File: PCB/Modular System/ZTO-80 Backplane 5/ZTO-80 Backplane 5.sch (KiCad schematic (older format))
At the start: 25 parts, among them J1 ZTO-80 Bus, J10 Conn_01x02, J11 PJ-102A, J12 Conn_01x02, J13 Conn_01x02, J2 Conn_01x02, J3 ZTO-80 Bus, J4 Conn_01x02, J5 ZTO-80 Bus, J6 Conn_01x02, J7 ZTO-80 Bus, J8 Conn_01x02, J9 ZTO-80 Bus, SW1 Reset

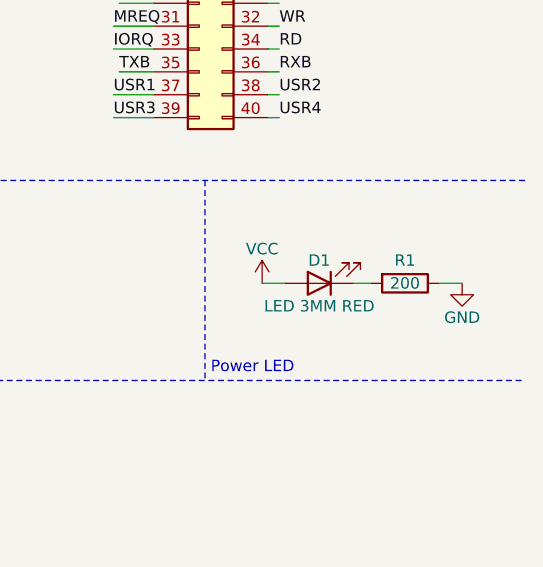
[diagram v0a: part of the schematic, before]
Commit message: Edited power LED resistor value
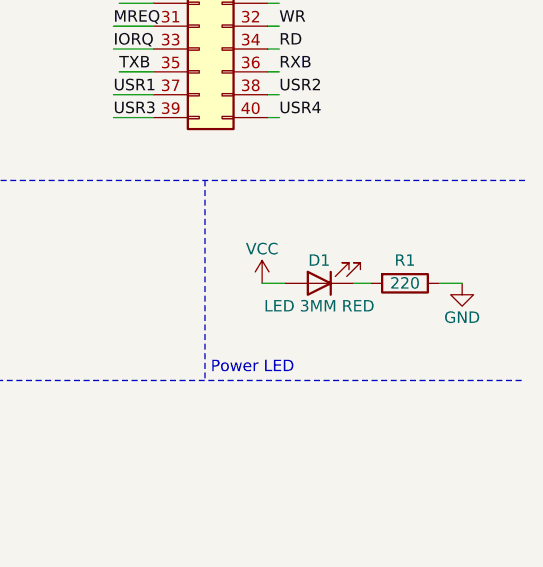
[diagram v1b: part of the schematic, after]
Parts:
- R1: value 200 -> 220
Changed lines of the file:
@@
 P 10700 3450
 F 0 "R1" V 10600 3450 50  0000 C CNN
-F 1 "200" V 10700 3450 50  0000 C CNN
+F 1 "220" V 10700 3450 50  0000 C CNN
 F 2 "Resistor_SMD:R_0805_2012Metric_Pad1.15x1.40mm_HandSolder" V 10630 3450 50  0001 C CNN
 F 3 "~" H 10700 3450 50  0001 C CNN

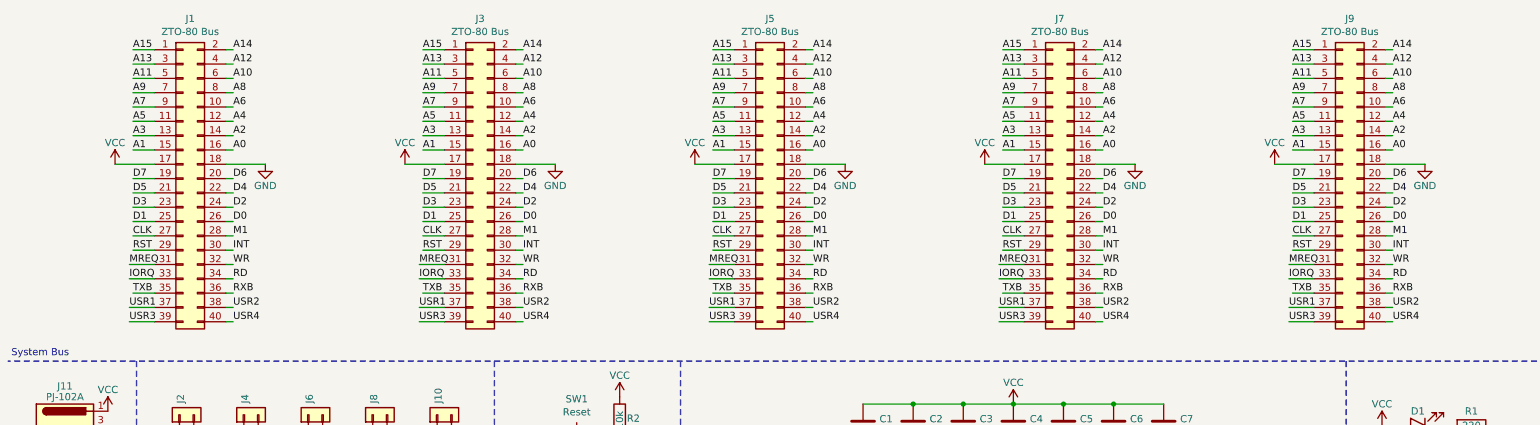
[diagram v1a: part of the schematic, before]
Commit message: Changed bus orientation
This change is backwards-compatible with all previous ZTO-80 modules
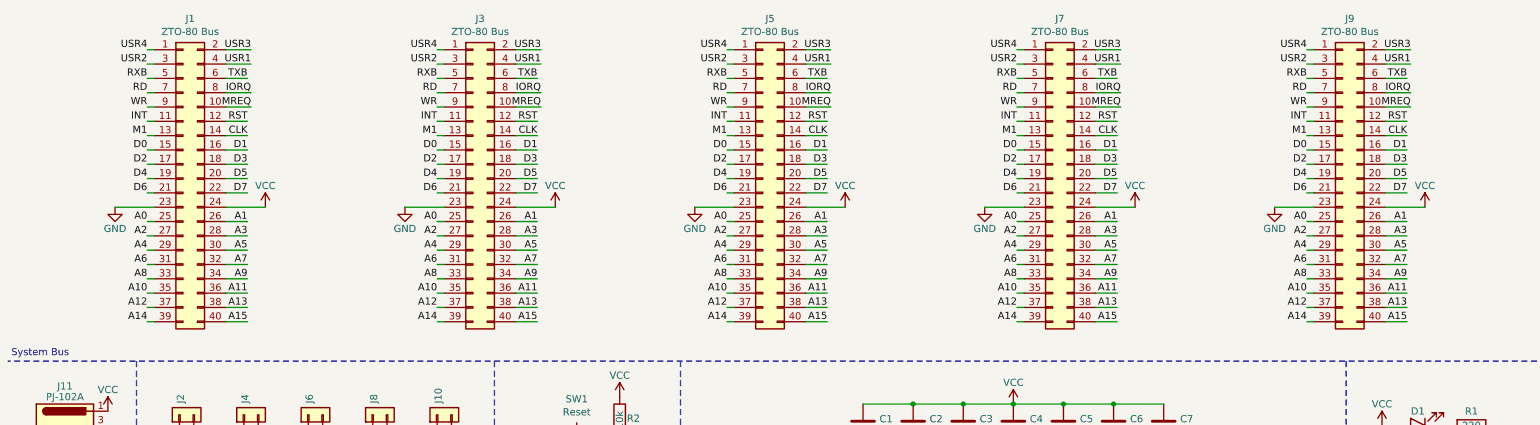
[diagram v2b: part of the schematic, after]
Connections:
- net A0: now also J1.25 (Pin_25), J3.25 (Pin_25), J5.25 (Pin_25), J7.25 (Pin_25), J9.25 (Pin_25); no longer J1.16 (Pin_16), J3.16 (Pin_16), J5.16 (Pin_16), J7.16 (Pin_16), J9.16 (Pin_16)
- net A1: now also J1.26 (Pin_26), J3.26 (Pin_26), J5.26 (Pin_26), J7.26 (Pin_26), J9.26 (Pin_26); no longer J1.15 (Pin_15), J3.15 (Pin_15), J5.15 (Pin_15), J7.15 (Pin_15), J9.15 (Pin_15)
- net A10: now also J1.35 (Pin_35), J3.35 (Pin_35), J5.35 (Pin_35), J7.35 (Pin_35), J9.35 (Pin_35); no longer J1.6 (Pin_6), J3.6 (Pin_6), J5.6 (Pin_6), J7.6 (Pin_6), J9.6 (Pin_6)
- net A11: now also J1.36 (Pin_36), J3.36 (Pin_36), J5.36 (Pin_36), J7.36 (Pin_36), J9.36 (Pin_36); no longer J1.5 (Pin_5), J3.5 (Pin_5), J5.5 (Pin_5), J7.5 (Pin_5), J9.5 (Pin_5)
- net A12: now also J1.37 (Pin_37), J3.37 (Pin_37), J5.37 (Pin_37), J7.37 (Pin_37), J9.37 (Pin_37); no longer J1.4 (Pin_4), J3.4 (Pin_4), J5.4 (Pin_4), J7.4 (Pin_4), J9.4 (Pin_4)
- net A13: now also J1.38 (Pin_38), J3.38 (Pin_38), J5.38 (Pin_38), J7.38 (Pin_38), J9.38 (Pin_38); no longer J1.3 (Pin_3), J3.3 (Pin_3), J5.3 (Pin_3), J7.3 (Pin_3), J9.3 (Pin_3)
- net A14: now also J1.39 (Pin_39), J3.39 (Pin_39), J5.39 (Pin_39), J7.39 (Pin_39), J9.39 (Pin_39); no longer J1.2 (Pin_2), J3.2 (Pin_2), J5.2 (Pin_2), J7.2 (Pin_2), J9.2 (Pin_2)
- net A15: now also J1.40 (Pin_40), J3.40 (Pin_40), J5.40 (Pin_40), J7.40 (Pin_40), J9.40 (Pin_40); no longer J1.1 (Pin_1), J3.1 (Pin_1), J5.1 (Pin_1), J7.1 (Pin_1), J9.1 (Pin_1)
- net A2: now also J1.27 (Pin_27), J3.27 (Pin_27), J5.27 (Pin_27), J7.27 (Pin_27), J9.27 (Pin_27); no longer J1.14 (Pin_14), J3.14 (Pin_14), J5.14 (Pin_14), J7.14 (Pin_14), J9.14 (Pin_14)
- net A3: now also J1.28 (Pin_28), J3.28 (Pin_28), J5.28 (Pin_28), J7.28 (Pin_28), J9.28 (Pin_28); no longer J1.13 (Pin_13), J3.13 (Pin_13), J5.13 (Pin_13), J7.13 (Pin_13), J9.13 (Pin_13)
- net A4: now also J1.29 (Pin_29), J3.29 (Pin_29), J5.29 (Pin_29), J7.29 (Pin_29), J9.29 (Pin_29); no longer J1.12 (Pin_12), J3.12 (Pin_12), J5.12 (Pin_12), J7.12 (Pin_12), J9.12 (Pin_12)
- net A5: now also J1.30 (Pin_30), J3.30 (Pin_30), J5.30 (Pin_30), J7.30 (Pin_30), J9.30 (Pin_30); no longer J1.11 (Pin_11), J3.11 (Pin_11), J5.11 (Pin_11), J7.11 (Pin_11), J9.11 (Pin_11)
- net A6: now also J1.31 (Pin_31), J3.31 (Pin_31), J5.31 (Pin_31), J7.31 (Pin_31), J9.31 (Pin_31); no longer J1.10 (Pin_10), J3.10 (Pin_10), J5.10 (Pin_10), J7.10 (Pin_10), J9.10 (Pin_10)
- net A7: now also J1.32 (Pin_32), J3.32 (Pin_32), J5.32 (Pin_32), J7.32 (Pin_32), J9.32 (Pin_32); no longer J1.9 (Pin_9), J3.9 (Pin_9), J5.9 (Pin_9), J7.9 (Pin_9), J9.9 (Pin_9)
- net A8: now also J1.33 (Pin_33), J3.33 (Pin_33), J5.33 (Pin_33), J7.33 (Pin_33), J9.33 (Pin_33); no longer J1.8 (Pin_8), J3.8 (Pin_8), J5.8 (Pin_8), J7.8 (Pin_8), J9.8 (Pin_8)
- net A9: now also J1.34 (Pin_34), J3.34 (Pin_34), J5.34 (Pin_34), J7.34 (Pin_34), J9.34 (Pin_34); no longer J1.7 (Pin_7), J3.7 (Pin_7), J5.7 (Pin_7), J7.7 (Pin_7), J9.7 (Pin_7)
- net CLK: now also J1.14 (Pin_14), J3.14 (Pin_14), J5.14 (Pin_14), J7.14 (Pin_14), J9.14 (Pin_14); no longer J1.27 (Pin_27), J3.27 (Pin_27), J5.27 (Pin_27), J7.27 (Pin_27), J9.27 (Pin_27)
- net D0: now also J1.15 (Pin_15), J3.15 (Pin_15), J5.15 (Pin_15), J7.15 (Pin_15), J9.15 (Pin_15); no longer J1.26 (Pin_26), J3.26 (Pin_26), J5.26 (Pin_26), J7.26 (Pin_26), J9.26 (Pin_26)
- net D1: now also J1.16 (Pin_16), J3.16 (Pin_16), J5.16 (Pin_16), J7.16 (Pin_16), J9.16 (Pin_16); no longer J1.25 (Pin_25), J3.25 (Pin_25), J5.25 (Pin_25), J7.25 (Pin_25), J9.25 (Pin_25)
- net D2: now also J1.17 (Pin_17), J3.17 (Pin_17), J5.17 (Pin_17), J7.17 (Pin_17), J9.17 (Pin_17); no longer J1.24 (Pin_24), J3.24 (Pin_24), J5.24 (Pin_24), J7.24 (Pin_24), J9.24 (Pin_24)
- net D3: now also J1.18 (Pin_18), J3.18 (Pin_18), J5.18 (Pin_18), J7.18 (Pin_18), J9.18 (Pin_18); no longer J1.23 (Pin_23), J3.23 (Pin_23), J5.23 (Pin_23), J7.23 (Pin_23), J9.23 (Pin_23)
- net D4: now also J1.19 (Pin_19), J3.19 (Pin_19), J5.19 (Pin_19), J7.19 (Pin_19), J9.19 (Pin_19); no longer J1.22 (Pin_22), J3.22 (Pin_22), J5.22 (Pin_22), J7.22 (Pin_22), J9.22 (Pin_22)
- net D5: now also J1.20 (Pin_20), J3.20 (Pin_20), J5.20 (Pin_20), J7.20 (Pin_20), J9.20 (Pin_20); no longer J1.21 (Pin_21), J3.21 (Pin_21), J5.21 (Pin_21), J7.21 (Pin_21), J9.21 (Pin_21)
- net D6: now also J1.21 (Pin_21), J3.21 (Pin_21), J5.21 (Pin_21), J7.21 (Pin_21), J9.21 (Pin_21); no longer J1.20 (Pin_20), J3.20 (Pin_20), J5.20 (Pin_20), J7.20 (Pin_20), J9.20 (Pin_20)
- net D7: now also J1.22 (Pin_22), J3.22 (Pin_22), J5.22 (Pin_22), J7.22 (Pin_22), J9.22 (Pin_22); no longer J1.19 (Pin_19), J3.19 (Pin_19), J5.19 (Pin_19), J7.19 (Pin_19), J9.19 (Pin_19)
- net GND: now also J1.23 (Pin_23), J3.23 (Pin_23), J5.23 (Pin_23), J7.23 (Pin_23), J9.23 (Pin_23); no longer J1.18 (Pin_18), J3.18 (Pin_18), J5.18 (Pin_18), J7.18 (Pin_18), J9.18 (Pin_18)
- net INT: now also J1.11 (Pin_11), J3.11 (Pin_11), J5.11 (Pin_11), J7.11 (Pin_11), J9.11 (Pin_11); no longer J1.30 (Pin_30), J3.30 (Pin_30), J5.30 (Pin_30), J7.30 (Pin_30), J9.30 (Pin_30)
- net IORQ: now also J1.8 (Pin_8), J3.8 (Pin_8), J5.8 (Pin_8), J7.8 (Pin_8), J9.8 (Pin_8); no longer J1.33 (Pin_33), J3.33 (Pin_33), J5.33 (Pin_33), J7.33 (Pin_33), J9.33 (Pin_33)
- net M1: now also J1.13 (Pin_13), J3.13 (Pin_13), J5.13 (Pin_13), J7.13 (Pin_13), J9.13 (Pin_13); no longer J1.28 (Pin_28), J3.28 (Pin_28), J5.28 (Pin_28), J7.28 (Pin_28), J9.28 (Pin_28)
- net MREQ: now also J1.10 (Pin_10), J3.10 (Pin_10), J5.10 (Pin_10), J7.10 (Pin_10), J9.10 (Pin_10); no longer J1.31 (Pin_31), J3.31 (Pin_31), J5.31 (Pin_31), J7.31 (Pin_31), J9.31 (Pin_31)
- net RD: now also J1.7 (Pin_7), J3.7 (Pin_7), J5.7 (Pin_7), J7.7 (Pin_7), J9.7 (Pin_7); no longer J1.34 (Pin_34), J3.34 (Pin_34), J5.34 (Pin_34), J7.34 (Pin_34), J9.34 (Pin_34)
- net RST: now also J1.12 (Pin_12), J3.12 (Pin_12), J5.12 (Pin_12), J7.12 (Pin_12), J9.12 (Pin_12); no longer J1.29 (Pin_29), J3.29 (Pin_29), J5.29 (Pin_29), J7.29 (Pin_29), J9.29 (Pin_29)
- net RXB: now also J1.5 (Pin_5), J3.5 (Pin_5), J5.5 (Pin_5), J7.5 (Pin_5), J9.5 (Pin_5); no longer J1.36 (Pin_36), J3.36 (Pin_36), J5.36 (Pin_36), J7.36 (Pin_36), J9.36 (Pin_36)
- net TXB: now also J1.6 (Pin_6), J3.6 (Pin_6), J5.6 (Pin_6), J7.6 (Pin_6), J9.6 (Pin_6); no longer J1.35 (Pin_35), J3.35 (Pin_35), J5.35 (Pin_35), J7.35 (Pin_35), J9.35 (Pin_35)
- net USR1: now also J1.4 (Pin_4), J3.4 (Pin_4), J5.4 (Pin_4), J7.4 (Pin_4), J9.4 (Pin_4); no longer J1.37 (Pin_37), J3.37 (Pin_37), J5.37 (Pin_37), J7.37 (Pin_37), J9.37 (Pin_37)
- net USR2: now also J1.3 (Pin_3), J3.3 (Pin_3), J5.3 (Pin_3), J7.3 (Pin_3), J9.3 (Pin_3); no longer J1.38 (Pin_38), J3.38 (Pin_38), J5.38 (Pin_38), J7.38 (Pin_38), J9.38 (Pin_38)
- net USR3: now also J1.2 (Pin_2), J3.2 (Pin_2), J5.2 (Pin_2), J7.2 (Pin_2), J9.2 (Pin_2); no longer J1.39 (Pin_39), J3.39 (Pin_39), J5.39 (Pin_39), J7.39 (Pin_39), J9.39 (Pin_39)
- net USR4: now also J1.1 (Pin_1), J3.1 (Pin_1), J5.1 (Pin_1), J7.1 (Pin_1), J9.1 (Pin_1); no longer J1.40 (Pin_40), J3.40 (Pin_40), J5.40 (Pin_40), J7.40 (Pin_40), J9.40 (Pin_40)
- net VCC: now also J1.24 (Pin_24), J3.24 (Pin_24), J5.24 (Pin_24), J7.24 (Pin_24), J9.24 (Pin_24); no longer J1.17 (Pin_17), J3.17 (Pin_17), J5.17 (Pin_17), J7.17 (Pin_17), J9.17 (Pin_17)
- net WR: now also J1.9 (Pin_9), J3.9 (Pin_9), J5.9 (Pin_9), J7.9 (Pin_9), J9.9 (Pin_9); no longer J1.32 (Pin_32), J3.32 (Pin_32), J5.32 (Pin_32), J7.32 (Pin_32), J9.32 (Pin_32)

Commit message: Updated Backplane
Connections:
- net VCC: now also J10.1 (Pin_1); no longer J2.1 (Pin_1)
- net at J2.2 (Pin_2): no longer J4.1 (Pin_1)
- net at J4.2 (Pin_2): now also J2.1 (Pin_1); no longer J6.1 (Pin_1)
- net at J6.2 (Pin_2): now also J4.1 (Pin_1); no longer J8.1 (Pin_1)
- net at J8.2 (Pin_2): now also J6.1 (Pin_1); no longer J10.1 (Pin_1)
- net at J10.2 (Pin_2): now also J8.1 (Pin_1)
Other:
- moved on the sheet: J10, J2, J4, J8
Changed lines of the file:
@@
 L Connector_Generic:Conn_01x02 J2
 U 1 1 5E36D3A1
-P 1675 3375
-F 0 "J2" H 1755 3367 50  0000 L CNN
-F 1 "Conn_01x02" H 1755 3276 50  0001 L CNN
-F 2 "Connector_PinSocket_2.54mm:PinSocket_2x01_P2.54mm_Vertical" H 1675 3375 50  0001 C CNN
-F 3 "~" H 1675 3375 50  0001 C CNN
-	1    1675 3375
+P 3475 3375
+F 0 "J2" H 3555 3367 50  0000 L CNN
+F 1 "Conn_01x02" H 3555 3276 50  0001 L CNN
+F 2 "Connector_PinSocket_2.54mm:PinSocket_2x01_P2.54mm_Vertical" H 3475 3375 50  0001 C CNN
+F 3 "~" H 3475 3375 50  0001 C CNN
+	1    3475 3375
 	0    -1   -1   0
 $EndComp
@@
 L Connector_Generic:Conn_01x02 J4
 U 1 1 5F1160A2
-P 2125 3375
-F 0 "J4" H 2205 3367 50  0000 L CNN
-F 1 "Conn_01x02" H 2205 3276 50  0001 L CNN
-F 2 "Connector_PinSocket_2.54mm:PinSocket_2x01_P2.54mm_Vertical" H 2125 3375 50  0001 C CNN
-F 3 "~" H 2125 3375 50  0001 C CNN
-	1    2125 3375
+P 3025 3375
+F 0 "J4" H 3105 3367 50  0000 L CNN
+F 1 "Conn_01x02" H 3105 3276 50  0001 L CNN
+F 2 "Connector_PinSocket_2.54mm:PinSocket_2x01_P2.54mm_Vertical" H 3025 3375 50  0001 C CNN
+F 3 "~" H 3025 3375 50  0001 C CNN
+	1    3025 3375
 	0    -1   -1   0
 $EndComp
@@
 L Connector_Generic:Conn_01x02 J8
 U 1 1 5F1335F2
-P 3025 3375
-F 0 "J8" H 3105 3367 50  0000 L CNN
-F 1 "Conn_01x02" H 3105 3276 50  0001 L CNN
-F 2 "Connector_PinSocket_2.54mm:PinSocket_2x01_P2.54mm_Vertical" H 3025 3375 50  0001 C CNN
-F 3 "~" H 3025 3375 50  0001 C CNN
-	1    3025 3375
+P 2125 3375
+F 0 "J8" H 2205 3367 50  0000 L CNN
+F 1 "Conn_01x02" H 2205 3276 50  0001 L CNN
+F 2 "Connector_PinSocket_2.54mm:PinSocket_2x01_P2.54mm_Vertical" H 2125 3375 50  0001 C CNN
+F 3 "~" H 2125 3375 50  0001 C CNN
+	1    2125 3375
 	0    -1   -1   0
 $EndComp
@@
 L Connector_Generic:Conn_01x02 J10
 U 1 1 5F14F000
-P 3475 3375
-F 0 "J10" H 3555 3367 50  0000 L CNN
-F 1 "Conn_01x02" H 3555 3276 50  0001 L CNN
-F 2 "Connector_PinSocket_2.54mm:PinSocket_2x01_P2.54mm_Vertical" H 3475 3375 50  0001 C CNN
-F 3 "~" H 3475 3375 50  0001 C CNN
-	1    3475 3375
+P 1675 3375
+F 0 "J10" H 1755 3367 50  0000 L CNN
+F 1 "Conn_01x02" H 1755 3276 50  0001 L CNN
+F 2 "Connector_PinSocket_2.54mm:PinSocket_2x01_P2.54mm_Vertical" H 1675 3375 50  0001 C CNN
+F 3 "~" H 1675 3375 50  0001 C CNN
+	1    1675 3375
 	0    -1   -1   0
 $EndComp
